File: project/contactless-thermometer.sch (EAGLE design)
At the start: 92 parts, among them J1 OLED, J2 ICSP, J3 BLE, J4 USB-MINIB-5PIN, Q1 MMBT3904, Q2 MMBT3904, Q3 ZXMP6A17GTA, U1 LT1167CS8#PBF, U2 OPA2705UA, U3 OPA705NA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

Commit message: Placement
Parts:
- C11, C12: value 0.1uF -> 22pF
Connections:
- net 5V: no longer C4.2
- net GND: now also C4.2
- net VIN: now also S1.3; no longer S1.1

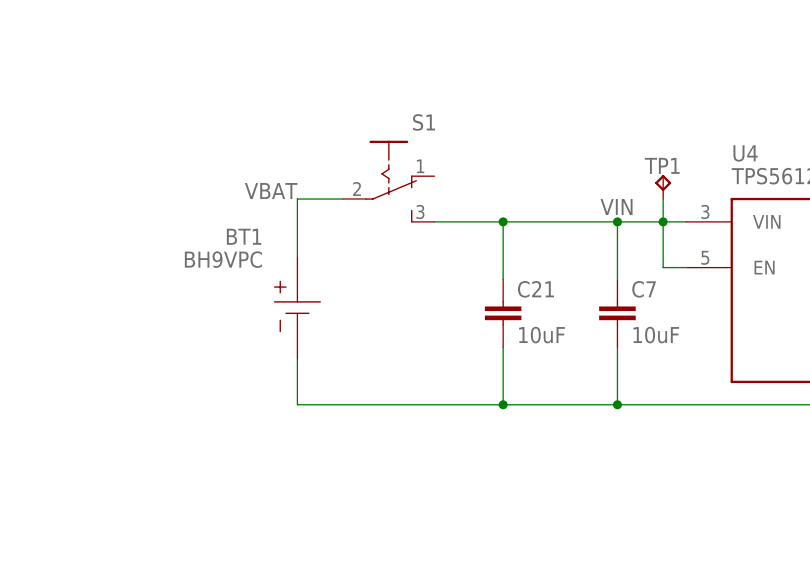
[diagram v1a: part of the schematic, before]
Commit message: alignment fix
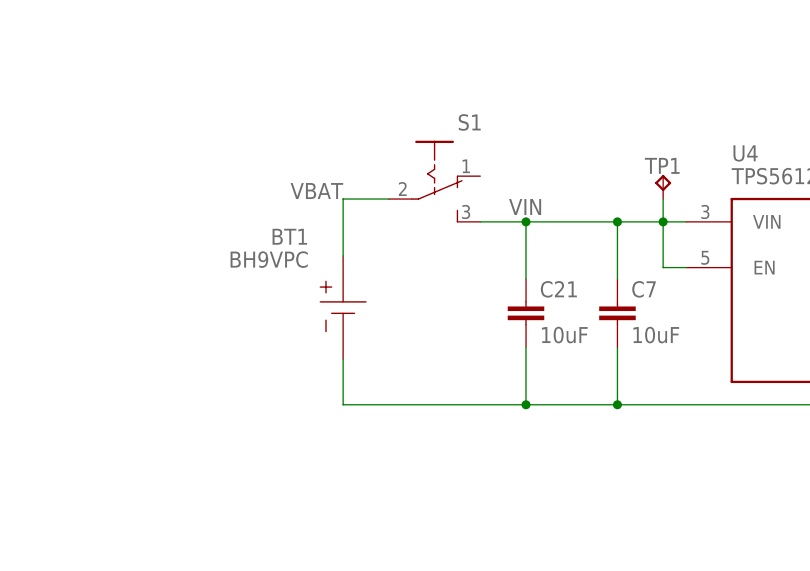
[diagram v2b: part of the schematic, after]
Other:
- moved on the sheet: BT1, C21, S1
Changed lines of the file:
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@@
 <setting verticaltext="up"/>
 </settings>
-<grid distance="0.1" unitdist="inch" unit="inch" style="lines" multiple="1" display="no" altdistance="0.01" altunitdist="inch" altunit="inch"/>
+<grid distance="0.1" unitdist="inch" unit="inch" style="lines" multiple="1" display="yes" altdistance="0.01" altunitdist="inch" altunit="inch"/>
 <layers>
 <layer number="1" name="Top" color="4" fill="1" visible="no" active="no"/>
@@
 <attribute name="VALUE" x="85.09" y="20.32" size="1.778" layer="96" align="center-left"/>
 </instance>
-<instance part="BT1" gate="G$1" x="-10.16" y="92.71" smashed="yes" rot="MR270" grouprefs="POWER">
-<attribute name="NAME" x="-13.97" y="93.98" size="1.778" layer="95" rot="MR0"/>
-<attribute name="VALUE" x="-13.97" y="91.44" size="1.778" layer="96" rot="MR0"/>
+<instance part="BT1" gate="G$1" x="-5.08" y="92.71" smashed="yes" rot="MR270" grouprefs="POWER">
+<attribute name="NAME" x="-8.89" y="93.98" size="1.778" layer="95" rot="MR0"/>
+<attribute name="VALUE" x="-8.89" y="91.44" size="1.778" layer="96" rot="MR0"/>
 </instance>
 <instance part="U4" gate="G$1" x="33.02" y="96.52" smashed="yes" grouprefs="POWER">
@@
 <attribute name="TP_SIGNAL_NAME" x="186.69" y="41.91" size="1.778" layer="97"/>
 </instance>
-<instance part="C21" gate="G$1" x="12.7" y="85.09" smashed="yes" rot="R90" grouprefs="POWER">
-<attribute name="NAME" x="14.22306875" y="88.138" size="1.778" layer="95"/>
-<attribute name="VALUE" x="14.23248125" y="83.058" size="1.778" layer="96"/>
-</instance>
-<instance part="S1" gate="A" x="-5.08" y="99.06" smashed="yes">
-<attribute name="NAME" x="2.54" y="106.68" size="1.778" layer="95" ratio="6" rot="SR0"/>
+<instance part="C21" gate="G$1" x="15.24" y="85.09" smashed="yes" rot="R90" grouprefs="POWER">
+<attribute name="NAME" x="16.76306875" y="88.138" size="1.778" layer="95"/>
+<attribute name="VALUE" x="16.77248125" y="83.058" size="1.778" layer="96"/>
+</instance>
+<instance part="S1" gate="A" x="0" y="99.06" smashed="yes">
+<attribute name="NAME" x="7.62" y="106.68" size="1.778" layer="95" ratio="6" rot="SR0"/>
 </instance>
 </instances>
@@
 <pinref part="BT1" gate="G$1" pin="-"/>
 <wire x1="93.98" y1="76.2" x2="101.6" y2="76.2" width="0.1524" layer="91" grouprefs="POWER"/>
-<wire x1="-10.16" y1="81.28" x2="-10.16" y2="76.2" width="0.1524" layer="91" grouprefs="POWER"/>
-<wire x1="-10.16" y1="76.2" x2="12.7" y2="76.2" width="0.1524" layer="91" grouprefs="POWER"/>
+<wire x1="-5.08" y1="81.28" x2="-5.08" y2="76.2" width="0.1524" layer="91" grouprefs="POWER"/>
+<wire x1="-5.08" y1="76.2" x2="15.24" y2="76.2" width="0.1524" layer="91" grouprefs="POWER"/>
 <junction x="60.96" y="76.2" grouprefs="POWER"/>
-<wire x1="12.7" y1="76.2" x2="25.4" y2="76.2" width="0.1524" layer="91" grouprefs="POWER"/>
+<wire x1="15.24" y1="76.2" x2="25.4" y2="76.2" width="0.1524" layer="91" grouprefs="POWER"/>
 <wire x1="25.4" y1="76.2" x2="60.96" y2="76.2" width="0.1524" layer="91" grouprefs="POWER"/>
 <wire x1="25.4" y1="82.55" x2="25.4" y2="76.2" width="0.1524" layer="91" grouprefs="POWER"/>
@@
 <pinref part="C9" gate="G$1" pin="2"/>
 <pinref part="C21" gate="G$1" pin="1"/>
-<wire x1="12.7" y1="82.55" x2="12.7" y2="76.2" width="0.1524" layer="91" grouprefs="POWER"/>
-<junction x="12.7" y="76.2" grouprefs="POWER"/>
+<wire x1="15.24" y1="82.55" x2="15.24" y2="76.2" width="0.1524" layer="91" grouprefs="POWER"/>
+<junction x="15.24" y="76.2" grouprefs="POWER"/>
 </segment>
 <segment>
@@
 <segment>
 <pinref part="U4" gate="G$1" pin="VIN"/>
-<wire x1="12.7" y1="96.52" x2="25.4" y2="96.52" width="0.1524" layer="91" grouprefs="POWER"/>
+<wire x1="15.24" y1="96.52" x2="25.4" y2="96.52" width="0.1524" layer="91" grouprefs="POWER"/>
 <wire x1="25.4" y1="96.52" x2="30.48" y2="96.52" width="0.1524" layer="91" grouprefs="POWER"/>
 <wire x1="30.48" y1="96.52" x2="33.02" y2="96.52" width="0.1524" layer="91" grouprefs="POWER"/>
 <wire x1="25.4" y1="90.17" x2="25.4" y2="96.52" width="0.1524" layer="91" grouprefs="POWER"/>
 <junction x="25.4" y="96.52" grouprefs="POWER"/>
-<label x="25.4" y="97.282" size="1.778" layer="95" align="bottom-center" grouprefs="POWER"/>
+<label x="15.24" y="97.282" size="1.778" layer="95" align="bottom-center" grouprefs="POWER"/>
 <pinref part="U4" gate="G$1" pin="EN"/>
 <wire x1="33.02" y1="91.44" x2="30.48" y2="91.44" width="0.1524" layer="91" grouprefs="POWER"/>
@@
 <pinref part="TP1" gate="G$1" pin="TP"/>
 <pinref part="C21" gate="G$1" pin="2"/>
-<wire x1="12.7" y1="90.17" x2="12.7" y2="96.52" width="0.1524" layer="91" grouprefs="POWER"/>
+<wire x1="15.24" y1="90.17" x2="15.24" y2="96.52" width="0.1524" layer="91" grouprefs="POWER"/>
 <pinref part="S1" gate="A" pin="3"/>
-<wire x1="5.08" y1="96.52" x2="12.7" y2="96.52" width="0.1524" layer="91"/>
-<junction x="12.7" y="96.52"/>
+<wire x1="10.16" y1="96.52" x2="15.24" y2="96.52" width="0.1524" layer="91"/>
+<junction x="15.24" y="96.52"/>
 </segment>
 </net>
@@
 <segment>
 <pinref part="BT1" gate="G$1" pin="+"/>
-<wire x1="-10.16" y1="92.71" x2="-10.16" y2="99.06" width="0.1524" layer="91" grouprefs="POWER"/>
-<wire x1="-10.16" y1="99.06" x2="-5.08" y2="99.06" width="0.1524" layer="91" grouprefs="POWER"/>
-<label x="-10.16" y="99.06" size="1.778" layer="95" rot="R180" align="top-left" grouprefs="POWER"/>
+<wire x1="-5.08" y1="92.71" x2="-5.08" y2="99.06" width="0.1524" layer="91" grouprefs="POWER"/>
+<wire x1="-5.08" y1="99.06" x2="0" y2="99.06" width="0.1524" layer="91" grouprefs="POWER"/>
+<label x="-5.08" y="99.06" size="1.778" layer="95" rot="R180" align="top-left" grouprefs="POWER"/>
 <pinref part="S1" gate="A" pin="2"/>
 </segment>

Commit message: PCB progress
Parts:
- added C22: 0.1uF, SparkFun-Capacitors:0.1UF-0603-25V-(+80/-20%)
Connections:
- net 3.3V: now also C22.1
- net GND: now also C22.2
- net N$15: now also U5.PB5(SCK); no longer U5.PB3(MOSI/OC2)
- net N$21: now also U5.PB3(MOSI/OC2); no longer U5.PB5(SCK)
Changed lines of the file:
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@@
 <part name="C21" library="GRM21BR6YA106KE43L" deviceset="GRM21BR6YA106KE43L" device="" value="10uF"/>
 <part name="S1" library="SK12F17G7" deviceset="SK12F17G7" device=""/>
+<part name="C22" library="SparkFun-Capacitors" deviceset="0.1UF" device="-0603-25V-(+80/-20%)" value="0.1uF"/>
+<part name="SUPPLY23" library="SparkFun-PowerSymbols" deviceset="3.3V" device=""/>
+<part name="SUPPLY41" library="supply2" library_urn="urn:adsk.eagle:library:372" deviceset="GND" device=""/>
 </parts>
 <sheets>
@@
 <attribute name="VALUE" x="337.058" y="14.478" size="1.778" layer="96" font="vector" align="top-left"/>
 </instance>
-<instance part="LED3" gate="G$1" x="327.66" y="-34.29" smashed="yes" rot="R90" grouprefs="LED MCU">
+<instance part="LED3" gate="G$1" x="327.66" y="-34.29" smashed="yes" rot="R90" grouprefs="MCU LED">
 <attribute name="NAME" x="324.104" y="-31.75" size="1.778" layer="95" rot="R90" align="bottom-center"/>
 <attribute name="VALUE" x="329.692" y="-31.75" size="1.778" layer="96" rot="R90" align="top-center"/>
@@
 <attribute name="VALUE" x="292.1" y="-59.944" size="1.778" layer="96" align="top-center"/>
 </instance>
-<instance part="SUPPLY24" gate="GND" x="327.66" y="-58.42" smashed="yes" grouprefs="LED MCU">
+<instance part="SUPPLY24" gate="GND" x="327.66" y="-58.42" smashed="yes" grouprefs="MCU LED">
 <attribute name="VALUE" x="327.66" y="-59.944" size="1.778" layer="96" align="top-center"/>
 </instance>
@@
 <attribute name="VALUE" x="293.624" y="-48.26" size="1.778" layer="96" rot="R90" align="top-center"/>
 </instance>
-<instance part="R24" gate="G$1" x="327.66" y="-48.26" smashed="yes" rot="R90" grouprefs="LED MCU">
+<instance part="R24" gate="G$1" x="327.66" y="-48.26" smashed="yes" rot="R90" grouprefs="MCU LED">
 <attribute name="NAME" x="326.136" y="-48.26" size="1.778" layer="95" rot="R90" align="bottom-center"/>
 <attribute name="VALUE" x="329.184" y="-48.26" size="1.778" layer="96" rot="R90" align="top-center"/>
@@
 <instance part="S1" gate="A" x="0" y="99.06" smashed="yes">
 <attribute name="NAME" x="7.62" y="106.68" size="1.778" layer="95" ratio="6" rot="SR0"/>
+</instance>
+<instance part="C22" gate="G$1" x="289.56" y="7.62" smashed="yes" rot="MR0">
+<attribute name="NAME" x="288.036" y="10.541" size="1.778" layer="95" rot="MR0"/>
+<attribute name="VALUE" x="288.036" y="5.461" size="1.778" layer="96" rot="MR0"/>
+</instance>
+<instance part="SUPPLY23" gate="G$1" x="289.56" y="15.24" smashed="yes">
+<attribute name="VALUE" x="289.56" y="18.034" size="1.778" layer="96" align="bottom-center"/>
+</instance>
+<instance part="SUPPLY41" gate="GND" x="289.56" y="0" smashed="yes">
+<attribute name="VALUE" x="289.56" y="-1.524" size="1.778" layer="96" align="top-center"/>
 </instance>
 </instances>
@@
 <segment>
 <pinref part="SUPPLY24" gate="GND" pin="GND"/>
-<wire x1="327.66" y1="-53.34" x2="327.66" y2="-55.88" width="0.1524" layer="91" grouprefs="LED MCU"/>
+<wire x1="327.66" y1="-53.34" x2="327.66" y2="-55.88" width="0.1524" layer="91" grouprefs="MCU LED"/>
 <pinref part="R24" gate="G$1" pin="1"/>
 </segment>
@@
 <wire x1="86.36" y1="43.18" x2="88.9" y2="43.18" width="0.1524" layer="91"/>
 </segment>
+<segment>
+<pinref part="SUPPLY41" gate="GND" pin="GND"/>
+<pinref part="C22" gate="G$1" pin="2"/>
+<wire x1="289.56" y1="2.54" x2="289.56" y2="5.08" width="0.1524" layer="91"/>
+</segment>
 </net>
 <net name="5V" class="0">
@@
 </segment>
 <segment>
-<pinref part="U5" gate="G$1" pin="PC0(ADC0)"/>
-<wire x1="325.12" y1="81.28" x2="327.66" y2="81.28" width="0.1524" layer="91" grouprefs="MCU"/>
 <label x="330.2" y="81.28" size="1.778" layer="95" align="center-left" grouprefs="MCU"/>
 <wire x1="327.66" y1="81.28" x2="330.2" y2="81.28" width="0.1524" layer="91" grouprefs="MCU"/>
 <wire x1="327.66" y1="83.82" x2="327.66" y2="81.28" width="0.1524" layer="91" grouprefs="MCU"/>
-<junction x="327.66" y="81.28" grouprefs="MCU"/>
 <pinref part="TP7" gate="G$1" pin="TP"/>
+<pinref part="U5" gate="G$1" pin="PC0(ADC0)"/>
+<wire x1="325.12" y1="81.28" x2="327.66" y2="81.28" width="0.1524" layer="91"/>
+<junction x="327.66" y="81.28"/>
 </segment>
 </net>
@@
 <pinref part="C19" gate="G$1" pin="1"/>
 </segment>
+<segment>
+<pinref part="C22" gate="G$1" pin="1"/>
+<wire x1="289.56" y1="12.7" x2="289.56" y2="15.24" width="0.1524" layer="91"/>
+<pinref part="SUPPLY23" gate="G$1" pin="3.3V"/>
+</segment>
 </net>
 <net name="RESET" class="0">
@@
 </segment>
 </net>
-<net name="N$15" class="0">
-<segment>
-<pinref part="U5" gate="G$1" pin="PB3(MOSI/OC2)"/>
-<wire x1="325.12" y1="27.94" x2="330.2" y2="27.94" width="0.1524" layer="91" grouprefs="MCU"/>
-<wire x1="330.2" y1="27.94" x2="330.2" y2="22.86" width="0.1524" layer="91" grouprefs="MCU"/>
-<pinref part="J2" gate="G$1" pin="1"/>
-<wire x1="330.2" y1="22.86" x2="332.74" y2="22.86" width="0.1524" layer="91" grouprefs="MCU"/>
-</segment>
-</net>
 <net name="N$19" class="0">
 <segment>
@@
 </segment>
 </net>
-<net name="N$21" class="0">
-<segment>
-<pinref part="U5" gate="G$1" pin="PB5(SCK)"/>
-<wire x1="325.12" y1="22.86" x2="325.12" y2="17.78" width="0.1524" layer="91" grouprefs="MCU"/>
-<pinref part="J2" gate="G$1" pin="5"/>
-<wire x1="325.12" y1="17.78" x2="332.74" y2="17.78" width="0.1524" layer="91" grouprefs="MCU"/>
-</segment>
-</net>
 <net name="LED_G" class="0">
 <segment>
 <pinref part="LED3" gate="G$1" pin="A"/>
-<wire x1="327.66" y1="-29.21" x2="327.66" y2="-22.86" width="0.1524" layer="91" grouprefs="LED MCU"/>
-<label x="327.66" y="-22.86" size="1.778" layer="95" rot="R90" align="center-left" grouprefs="LED MCU"/>
+<wire x1="327.66" y1="-29.21" x2="327.66" y2="-22.86" width="0.1524" layer="91" grouprefs="MCU LED"/>
+<label x="327.66" y="-22.86" size="1.778" layer="95" rot="R90" align="center-left" grouprefs="MCU LED"/>
 </segment>
 <segment>
@@
 <segment>
 <pinref part="LED3" gate="G$1" pin="K"/>
-<wire x1="327.66" y1="-34.29" x2="327.66" y2="-43.18" width="0.1524" layer="91" grouprefs="LED MCU"/>
+<wire x1="327.66" y1="-34.29" x2="327.66" y2="-43.18" width="0.1524" layer="91" grouprefs="MCU LED"/>
 <pinref part="R24" gate="G$1" pin="2"/>
 </segment>
@@
 </segment>
 </net>
+<net name="N$15" class="0">
+<segment>
+<pinref part="U5" gate="G$1" pin="PB5(SCK)"/>
+<pinref part="J2" gate="G$1" pin="1"/>
+<wire x1="325.12" y1="22.86" x2="332.74" y2="22.86" width="0.1524" layer="91"/>
+</segment>
+</net>
+<net name="N$21" class="0">
+<segment>
+<pinref part="U5" gate="G$1" pin="PB3(MOSI/OC2)"/>
+<wire x1="325.12" y1="27.94" x2="330.2" y2="27.94" width="0.1524" layer="91"/>
+<wire x1="330.2" y1="27.94" x2="330.2" y2="17.78" width="0.1524" layer="91"/>
+<pinref part="J2" gate="G$1" pin="5"/>
+<wire x1="330.2" y1="17.78" x2="332.74" y2="17.78" width="0.1524" layer="91"/>
+</segment>
+</net>

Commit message: allah
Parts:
- removed TP3: TPTP10R, testpad:TPTP10R
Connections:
- net 2.5V: no longer TP3.TP
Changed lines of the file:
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@@
 <part name="TP1" library="testpad" library_urn="urn:adsk.eagle:library:385" deviceset="TP" device="TP10R" package3d_urn="urn:adsk.eagle:package:27959/1"/>
 <part name="TP2" library="testpad" library_urn="urn:adsk.eagle:library:385" deviceset="TP" device="TP10R" package3d_urn="urn:adsk.eagle:package:27959/1"/>
-<part name="TP3" library="testpad" library_urn="urn:adsk.eagle:library:385" deviceset="TP" device="TP10R" package3d_urn="urn:adsk.eagle:package:27959/1"/>
 <part name="TP4" library="testpad" library_urn="urn:adsk.eagle:library:385" deviceset="TP" device="TP10R" package3d_urn="urn:adsk.eagle:package:27959/1"/>
 <part name="TP5" library="testpad" library_urn="urn:adsk.eagle:library:385" deviceset="TP" device="TP10R" package3d_urn="urn:adsk.eagle:package:27959/1"/>
@@
 <attribute name="NAME" x="101.6" y="101.854" size="1.778" layer="95" align="bottom-center"/>
 <attribute name="TP_SIGNAL_NAME" x="102.87" y="100.33" size="1.778" layer="97"/>
-</instance>
-<instance part="TP3" gate="G$1" x="121.92" y="91.44" smashed="yes" grouprefs="POWER">
-<attribute name="NAME" x="121.92" y="91.694" size="1.778" layer="95" align="bottom-center"/>
-<attribute name="TP_SIGNAL_NAME" x="123.19" y="90.17" size="1.778" layer="97"/>
 </instance>
 <instance part="TP4" gate="G$1" x="177.8" y="81.28" smashed="yes" rot="R180" grouprefs="POWER">
@@
 <segment>
 <pinref part="U3" gate="G$1" pin="+IN"/>
-<wire x1="127" y1="86.36" x2="121.92" y2="86.36" width="0.1524" layer="91" grouprefs="POWER"/>
+<wire x1="127" y1="86.36" x2="119.38" y2="86.36" width="0.1524" layer="91" grouprefs="POWER"/>
 <label x="119.38" y="86.36" size="1.778" layer="95" rot="R180" xref="yes" grouprefs="POWER"/>
-<wire x1="121.92" y1="86.36" x2="119.38" y2="86.36" width="0.1524" layer="91" grouprefs="POWER"/>
-<wire x1="121.92" y1="88.9" x2="121.92" y2="86.36" width="0.1524" layer="91" grouprefs="POWER"/>
-<junction x="121.92" y="86.36" grouprefs="POWER"/>
-<pinref part="TP3" gate="G$1" pin="TP"/>
-</segment>
-<segment>
+</segment>
+<segment>
